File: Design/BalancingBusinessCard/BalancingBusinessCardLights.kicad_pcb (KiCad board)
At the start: 2 copper layers, 51 x 89 mm, 40 parts, among them SW101 SW_SPST, U101 ATtiny261A-MU, U401 LIS3DHTR

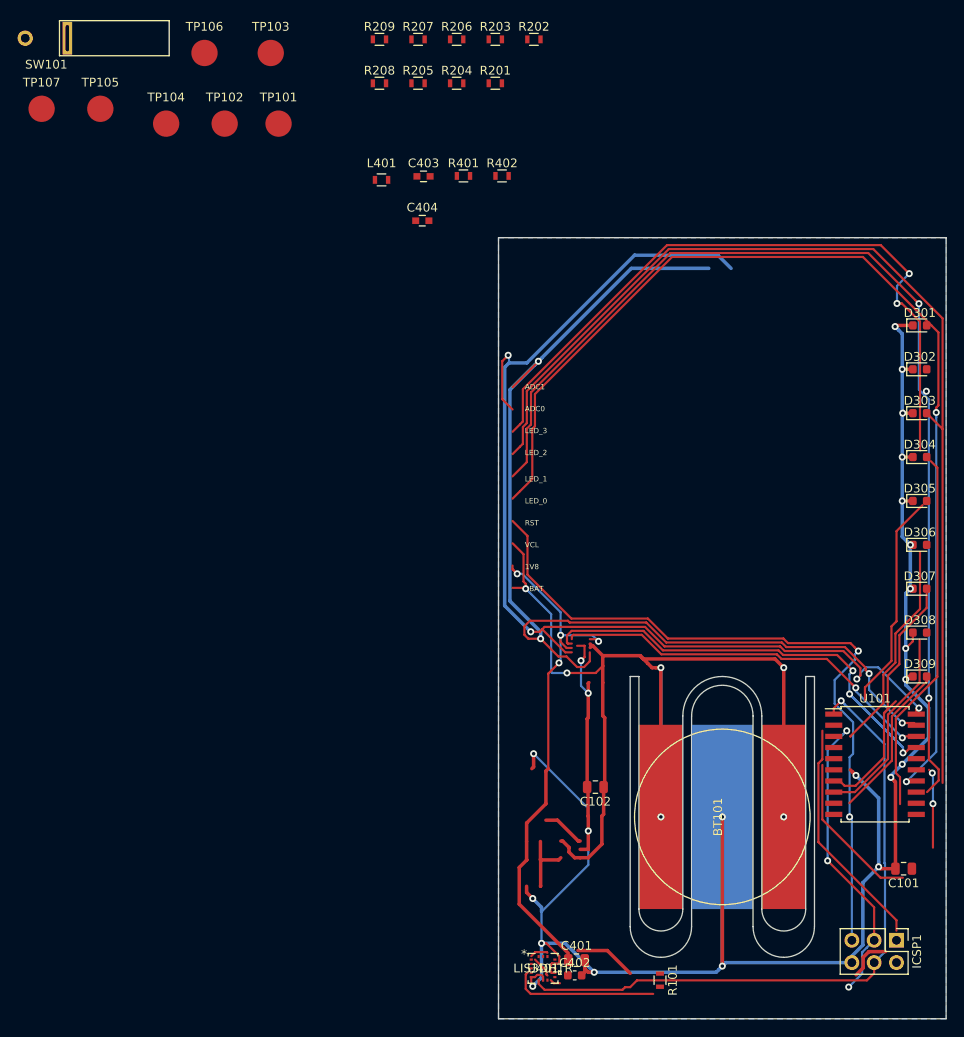
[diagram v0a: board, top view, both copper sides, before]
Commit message: Finished light board layout and silkscreen design
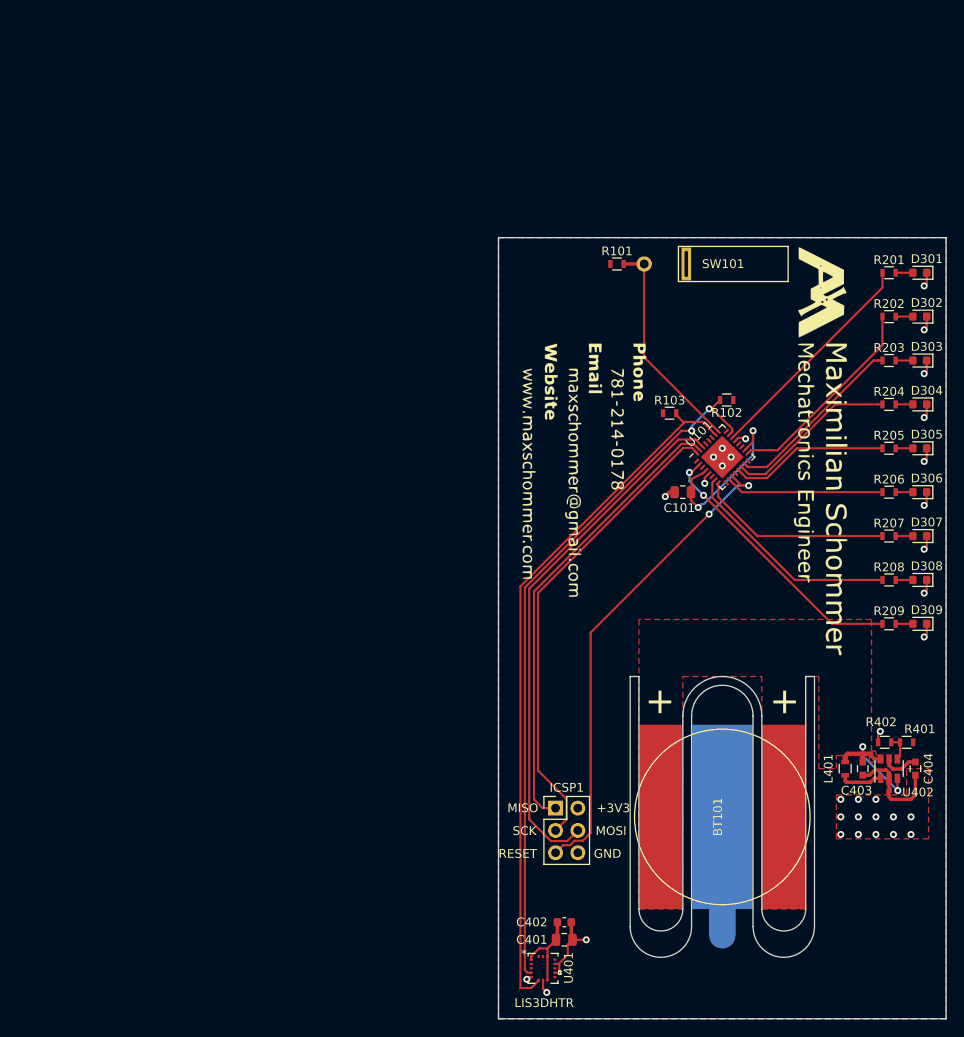
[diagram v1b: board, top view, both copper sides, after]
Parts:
- removed C102: 10uF, Capacitor_SMD:C_0805_2012Metric
- removed TP101: BATT_TP, Measurement_Points:Measurement_Point_Round-SMD-Pad_Big
- removed TP102: 3V3_TP, Measurement_Points:Measurement_Point_Round-SMD-Pad_Big
- removed TP103: RESET_TP, Measurement_Points:Measurement_Point_Round-SMD-Pad_Big
- removed TP104: LED_0_TP, Measurement_Points:Measurement_Point_Round-SMD-Pad_Big
- removed TP105: LED_1_TP, Measurement_Points:Measurement_Point_Round-SMD-Pad_Big
- removed TP106: LED_2_TP, Measurement_Points:Measurement_Point_Round-SMD-Pad_Big
- removed TP107: TILT_TP, Measurement_Points:Measurement_Point_Round-SMD-Pad_Big
- added G***: LOGO, CustomFootprints:MaxCardSilkscreen, F.Cu at (205.6, 94.5)
- added R102: 10k, Resistors_SMD:R_0603, F.Cu at (206.0, 68.5)
- added R103: 10k, Resistors_SMD:R_0603, F.Cu at (199.5, 70.0)
- added U402: MCP1640DCH, TO_SOT_Packages_SMD:SOT-23-6, F.Cu at (224.5, 110.5)
- U101: footprint Package_SO:SOIC-20W_7.5x12.8mm_P1.27mm -> Housings_DFN_QFN:QFN-32-1EP_5x5mm_Pitch0.5mm
- moved R209 88.4 mm to (224.5, 94.0)
- moved L401 85.4 mm to (219.5, 110.5), turned to 90 degrees
- moved C403 84.0 mm to (221.5, 110.5), turned to 270 degrees
- moved C404 84.0 mm to (227.5, 110.5), turned to 270 degrees
- moved R401 81.9 mm to (226.5, 107.5), turned to 180 degrees
- moved R101 81.7 mm to (193.5, 53.0), turned to 0 degrees
- moved R208 81.1 mm to (224.5, 89.0)
- moved R207 78.0 mm to (224.5, 84.0)
- moved R402 77.9 mm to (224.0, 107.5), turned to 180 degrees
- moved SW101 75.1 mm to (199.0, 53.0)
- moved R206 71.3 mm to (224.5, 79.0)
- moved R205 67.9 mm to (224.5, 74.0)
- moved R204 61.4 mm to (224.5, 69.0)
- moved R203 57.9 mm to (224.5, 64.0)
- moved R202 51.3 mm to (224.5, 59.0)
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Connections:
- ICSP1 pad 1: (no net) -> /MISO
- ICSP1 pad 4: (no net) -> /MOSI
- L401 pad 1: (no net) -> Net-(L401-Pad1)
- U101 pad 1: (no net) -> Net-(U101-Pad1)
- U101 pad 10: /LED_8 -> /LED_5
- U101 pad 12: (no net) -> Net-(U101-Pad12)
- U101 pad 16: (no net) -> Net-(U101-Pad16)
- U101 pad 19: (no net) -> Net-(U101-Pad19)
- U101 pad 2: /LED_5 -> /LED_8
- U101 pad 20: (no net) -> Net-(U101-Pad20)
- U101 pad 3: (no net) -> Net-(U101-Pad3)
- U101 pad 6: (no net) -> Net-(U101-Pad6)
- U101 pad 7: /LED_6 -> /LED_7
- U101 pad 8: /LED_7 -> /LED_6
- U101 pad 9: (no net) -> Net-(U101-Pad9)
- U401 pad 11: (no net) -> Net-(U401-Pad11)
- U401 pad 13: (no net) -> Net-(U401-Pad13)
- U401 pad 15: (no net) -> Net-(U401-Pad15)
- U401 pad 16: (no net) -> Net-(U401-Pad16)
- U401 pad 2: (no net) -> Net-(U401-Pad2)
- U401 pad 3: (no net) -> Net-(U401-Pad3)
- U401 pad 4: (no net) -> /SCL
- U401 pad 6: (no net) -> /SDA
- U401 pad 9: (no net) -> Net-(U401-Pad9)
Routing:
- net (no net): track 327.1 -> 0.00 mm, vias 9 -> 0
- net GND: track 250.6 -> 56.3 mm, vias 23 -> 33
- net /LED_1: track 179.7 -> 23.7 mm, vias 6 -> 0
- net /LED_0: track 121.7 -> 0.00 mm, vias 2 -> 0
- net Net-(D303-Pad2): track 120.7 -> 1.96 mm
- net +BATT: track 129.8 -> 16.1 mm, vias 6 -> 2
- net +1V8: track 104.1 -> 0.00 mm, vias 6 -> 0
- net /LED_3: track 121.2 -> 19.6 mm, vias 2 -> 0
- net /SDA: track 0.00 -> 80.6 mm
- net /SCL: track 0.00 -> 80.2 mm, vias 0 -> 2
- net /MOSI: track 0.00 -> 60.5 mm
- net /MISO: track 0.00 -> 52.7 mm
- net /LED_4: track 51.6 -> 18.1 mm
- net /LED_8: track 0.00 -> 31.3 mm, vias 0 -> 2
- net /RESET: track 83.3 -> 55.0 mm
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- added copper zone on F.Cu, net +3V3
- added copper zone on F.Cu, net +BATT
- added copper zone on F.Cu, net GND
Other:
- board text added: "+"
- board text added: "+3V3"
- board text added: "-"
- board text added: "GND"
- board text added: "MISO"
- board text added: "MOSI"
- board text added: "RESET"
- board text added: "SCK"
- board text removed: "1V8"
- board text removed: "ADC0"
- board text removed: "ADC1"
- board text removed: "BAT"
- board text removed: "LED_0"
- board text removed: "LED_1"
- board text removed: "LED_2"
- board text removed: "LED_3"
- board text removed: "RST"
- board text removed: "VCL"

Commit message: Rev2 Shipped
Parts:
- removed the G*** at (205.6, 94.5)
- added G***: LOGO, CustomFootprints:EricCardSilkscreen, F.Cu at (205.5, 94.5)
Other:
- outline, holes or cut-outs redrawn

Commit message: Began v3 board design
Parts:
- removed G***: LOGO, CustomFootprints:EricCardSilkscreen
- added J101: Conn_02x01, Connector_PinHeader_2.54mm:PinHeader_1x02_P2.54mm_Vertical, F.Cu at (206.6, 51.9)
- added TP101: TestPoint, TestPoint:TestPoint_Pad_D3.0mm, F.Cu at (183.4, 78.5)
- added TP102: TestPoint, TestPoint:TestPoint_Pad_D3.0mm, F.Cu at (183.4, 72.2)
- R101: value 10k -> 976k; footprint Resistors_SMD:R_0603 -> Resistor_SMD:R_0603_1608Metric
- SW101: value SW_SPST -> SW_Push; footprint CustomFootprints:RB-231X2 -> CustomFootprints:TouchButton1
- moved SW101 10.3 mm to (190.0, 57.9)
- moved R101 5.68 mm to (199.1, 52.1)
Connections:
- net /DEBUG renamed /LED_0
- R101 pad 1: +3V3 -> /TOUCH
- R101 pad 2: /TILT -> +3V3
- SW101 pad 1: /TILT -> /TOUCH
- U101 pad 1: Net-(U101-Pad1) -> (no net)
- U101 pad 12: Net-(U101-Pad12) -> (no net)
- U101 pad 16: Net-(U101-Pad16) -> (no net)
- U101 pad 19: Net-(U101-Pad19) -> (no net)
- U101 pad 20: Net-(U101-Pad20) -> (no net)
- U101 pad 24: Net-(U101-Pad24) -> (no net)
- U101 pad 25: /TILT -> /TOUCH
- U101 pad 27: Net-(U101-Pad27) -> (no net)
- U101 pad 28: Net-(U101-Pad28) -> (no net)
- U101 pad 29: Net-(U101-Pad29) -> (no net)
- U101 pad 3: Net-(U101-Pad3) -> (no net)
- U101 pad 6: Net-(U101-Pad6) -> (no net)
- U101 pad 9: Net-(U101-Pad9) -> (no net)
- U401 pad 11: Net-(U401-Pad11) -> (no net)
- U401 pad 13: Net-(U401-Pad13) -> (no net)
- U401 pad 15: Net-(U401-Pad15) -> (no net)
- U401 pad 16: Net-(U401-Pad16) -> (no net)
- U401 pad 2: Net-(U401-Pad2) -> (no net)
- U401 pad 3: Net-(U401-Pad3) -> (no net)
- U401 pad 9: Net-(U401-Pad9) -> (no net)
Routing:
- net /TILT: track 24.9 -> 0.00 mm

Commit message: Basic layout for v3
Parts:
- moved TP101 6.85 mm to (184.2, 71.7)
- moved TP102 6.68 mm to (184.4, 78.8)
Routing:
- net /TOUCH: track 0.00 -> 41.0 mm
- net GND: track 56.3 -> 76.0 mm, vias 33 -> 34
- net /SDA: track 80.6 -> 91.6 mm
- net /SCL: track 80.2 -> 86.3 mm
- net +3V3: track 33.5 -> 37.7 mm
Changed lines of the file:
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@@
     (thickness 1.6)
     (drawings 36)
-    (tracks 255)
+    (tracks 284)
     (zones 0)
     (modules 38)
@@
       (net 29 /TOUCH))
   )
-  (module TestPoint:TestPoint_Pad_D3.0mm (layer F.Cu)
-    (at 183.4 78.5)
+  (module TestPoint:TestPoint_Pad_D3.0mm locked (layer F.Cu)
+    (at 184.2 71.7)
     (descr "SMD pad as test Point, diameter 3.0mm")
     (tags "test point SMD pad")
@@
   )
   (module TestPoint:TestPoint_Pad_D3.0mm (layer F.Cu)
-    (at 183.4 72.2)
+    (at 184.4 78.8)
     (descr "SMD pad as test Point, diameter 3.0mm")
     (tags "test point SMD pad")
@@
   (segment (start 200.0625 79) (end 199.475 79) (width 0.4) (layer F.Cu) (net 2) (status 10))
   (segment (start 205.5 116) (end 205.5 129.5) (width 3) (layer B.Cu) (net 2) (status 10))
+  (via (at 197.3 54.6) (size 0.8) (drill 0.4) (layers F.Cu B.Cu) (net 2))
+  (segment (start 193.225 54.566667) (end 197.266667 54.566667) (width 0.25) (layer F.Cu) (net 2))
+  (segment (start 197.266667 54.566667) (end 197.3 54.6) (width 0.25) (layer F.Cu) (net 2))
+  (segment (start 193.225 54.566667) (end 190.225 54.566667) (width 0.25) (layer F.Cu) (net 2))
+  (segment (start 193.225 57.9) (end 190.225 57.9) (width 0.25) (layer F.Cu) (net 2))
+  (segment (start 193.225 61.233333) (end 190.225 61.233333) (width 0.25) (layer F.Cu) (net 2))
+  (segment (start 193.225 61.233333) (end 193.225 57.9) (width 0.25) (layer F.Cu) (net 2))
+  (segment (start 193.225 57.9) (end 193.225 54.566667) (width 0.25) (layer F.Cu) (net 2))
   (segment (start 208.75269 74.222184) (end 208.434493 74.540381) (width 0.25) (layer F.Cu) (net 3) (status 20))
   (segment (start 211.777816 74.222184) (end 208.75269 74.222184) (width 0.25) (layer F.Cu) (net 3))
@@
   (segment (start 209 74.75) (end 209 72) (width 0.25) (layer B.Cu) (net 13))
   (segment (start 203.399999 80.350001) (end 209 74.75) (width 0.25) (layer B.Cu) (net 13))
+  (segment (start 203.86 52.1) (end 204.06 51.9) (width 0.25) (layer F.Cu) (net 13))
+  (segment (start 199.9 52.1) (end 203.86 52.1) (width 0.25) (layer F.Cu) (net 13))
   (segment (start 225.25 54) (end 227.2125 54) (width 0.25) (layer F.Cu) (net 14) (status 30))
   (segment (start 225.25 59) (end 227.2125 59) (width 0.25) (layer F.Cu) (net 15) (status 30))
@@
   (segment (start 201.05 71) (end 200.25 70.2) (width 0.25) (layer F.Cu) (net 27) (status 20))
   (segment (start 201.5 71) (end 201.05 71) (width 0.25) (layer F.Cu) (net 27))
-  (segment (start 184.575002 134.601201) (end 184.575002 134.652001) (width 0.25) (layer F.Cu) (net 27) (status 30))
-  (segment (start 182.5 89.727178) (end 201.227178 71) (width 0.25) (layer F.Cu) (net 27))
+  (segment (start 188.5 71) (end 201.5 71) (width 0.25) (layer F.Cu) (net 27))
+  (segment (start 182.5 135.5) (end 182.5 77) (width 0.25) (layer F.Cu) (net 27))
   (segment (start 183.727003 135.5) (end 182.5 135.5) (width 0.25) (layer F.Cu) (net 27))
-  (segment (start 201.227178 71) (end 201.5 71) (width 0.25) (layer F.Cu) (net 27))
-  (segment (start 182.5 135.5) (end 182.5 89.727178) (width 0.25) (layer F.Cu) (net 27))
-  (segment (start 184.575002 134.652001) (end 183.727003 135.5) (width 0.25) (layer F.Cu) (net 27) (status 10))
+  (segment (start 184.575002 134.601201) (end 184.575002 134.652001) (width 0.25) (layer F.Cu) (net 27))
+  (segment (start 184.575002 134.652001) (end 183.727003 135.5) (width 0.25) (layer F.Cu) (net 27))
+  (segment (start 184.2 71.7) (end 187.8 71.7) (width 0.25) (layer F.Cu) (net 27))
+  (segment (start 182.5 77) (end 187.8 71.7) (width 0.25) (layer F.Cu) (net 27))
+  (segment (start 187.8 71.7) (end 188.5 71) (width 0.25) (layer F.Cu) (net 27))
   (via (at 204 69.5) (size 0.8) (drill 0.4) (layers F.Cu B.Cu) (net 28))
   (segment (start 204.348722 69.5) (end 204 69.5) (width 0.25) (layer F.Cu) (net 28))
@@
   (segment (start 202.012672 71.487328) (end 202.012672 72.012647) (width 0.25) (layer B.Cu) (net 28))
   (segment (start 204 69.5) (end 202.012672 71.487328) (width 0.25) (layer B.Cu) (net 28))
-  (segment (start 183 133.453999) (end 183 89.863589) (width 0.25) (layer F.Cu) (net 28))
-  (segment (start 200.850942 72.012647) (end 201.446987 72.012647) (width 0.25) (layer F.Cu) (net 28))
+  (segment (start 194.487353 72.012647) (end 201.446987 72.012647) (width 0.25) (layer F.Cu) (net 28))
+  (segment (start 183 133.453999) (end 183 83.5) (width 0.25) (layer F.Cu) (net 28))
+  (segment (start 183.728801 133.755) (end 183.301001 133.755) (width 0.25) (layer F.Cu) (net 28))
+  (segment (start 201.446987 72.012647) (end 202.012672 72.012647) (width 0.25) (layer F.Cu) (net 28))
   (segment (start 183.301001 133.755) (end 183 133.453999) (width 0.25) (layer F.Cu) (net 28))
-  (segment (start 183.728801 133.755) (end 183.301001 133.755) (width 0.25) (layer F.Cu) (net 28) (status 10))
-  (segment (start 201.446987 72.012647) (end 202.012672 72.012647) (width 0.25) (layer F.Cu) (net 28))
-  (segment (start 183 89.863589) (end 200.850942 72.012647) (width 0.25) (layer F.Cu) (net 28))
+  (segment (start 186 80.4) (end 186 80.5) (width 0.25) (layer F.Cu) (net 28))
+  (segment (start 184.4 78.8) (end 186 80.4) (width 0.25) (layer F.Cu) (net 28))
+  (segment (start 183 83.5) (end 186 80.5) (width 0.25) (layer F.Cu) (net 28))
+  (segment (start 186 80.5) (end 194.487353 72.012647) (width 0.25) (layer F.Cu) (net 28))
+  (segment (start 189.504043 62.970709) (end 188.6 62.066666) (width 0.25) (layer F.Cu) (net 29))
+  (segment (start 195.758333 69.224999) (end 189.504043 62.970709) (width 0.25) (layer F.Cu) (net 29))
+  (segment (start 202.199873 69.224999) (end 195.758333 69.224999) (width 0.25) (layer F.Cu) (net 29))
+  (segment (start 205.040381 72.065507) (end 202.199873 69.224999) (width 0.25) (layer F.Cu) (net 29))
+  (segment (start 187.766666 61.233333) (end 188.6 60.399999) (width 0.25) (layer F.Cu) (net 29))
+  (segment (start 186.725 61.233333) (end 187.766666 61.233333) (width 0.25) (layer F.Cu) (net 29))
+  (segment (start 188.6 60.399999) (end 188.6 58.733333) (width 0.25) (layer F.Cu) (net 29))
+  (segment (start 187.766666 57.9) (end 188.6 57.066666) (width 0.25) (layer F.Cu) (net 29))
+  (segment (start 186.725 57.9) (end 187.766666 57.9) (width 0.25) (layer F.Cu) (net 29))
+  (segment (start 188.6 57.066666) (end 188.6 55.4) (width 0.25) (layer F.Cu) (net 29))
+  (segment (start 187.766666 54.566667) (end 188.6 53.733333) (width 0.25) (layer F.Cu) (net 29))
+  (segment (start 186.725 54.566667) (end 187.766666 54.566667) (width 0.25) (layer F.Cu) (net 29))
+  (segment (start 190.233333 52.1) (end 198.325 52.1) (width 0.25) (layer F.Cu) (net 29))
+  (segment (start 188.6 53.733333) (end 190.233333 52.1) (width 0.25) (layer F.Cu) (net 29))
   (zone (net 2) (net_name GND) (layer B.Cu) (hatch edge 0.508)
     (connect_pads (clearance 0.508))
